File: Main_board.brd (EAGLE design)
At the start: 77.5 x 67.3 mm, 77 parts, among them IC1 4050D, U1 MCP73831, U2 TPS61200, U3 MAX1704X, U4 USD-SOCKETNEW, U5 TPS61200, X1 USB-MICROB, Y1 16MHz KX-7

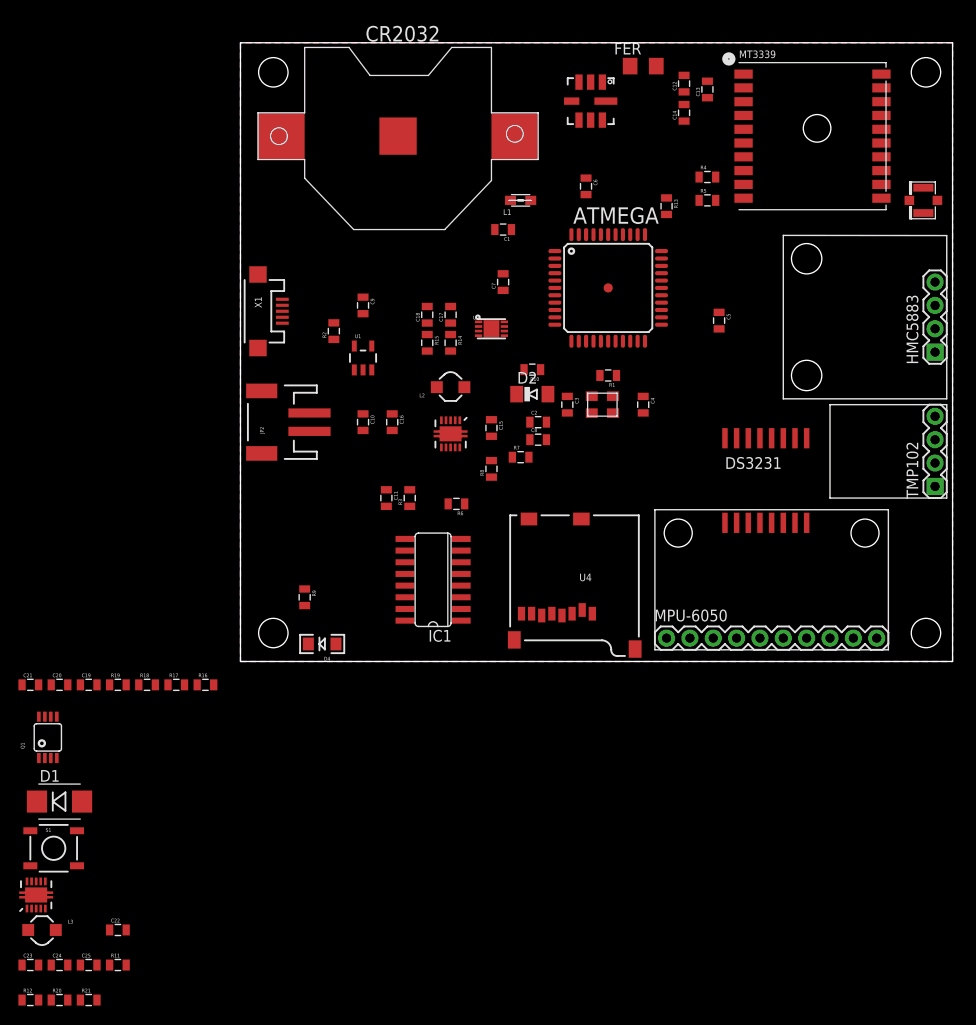
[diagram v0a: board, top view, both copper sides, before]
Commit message: Big update
Replacement of old file by only one unique file
Reorganisation of schematics
Integration of the screen footprint
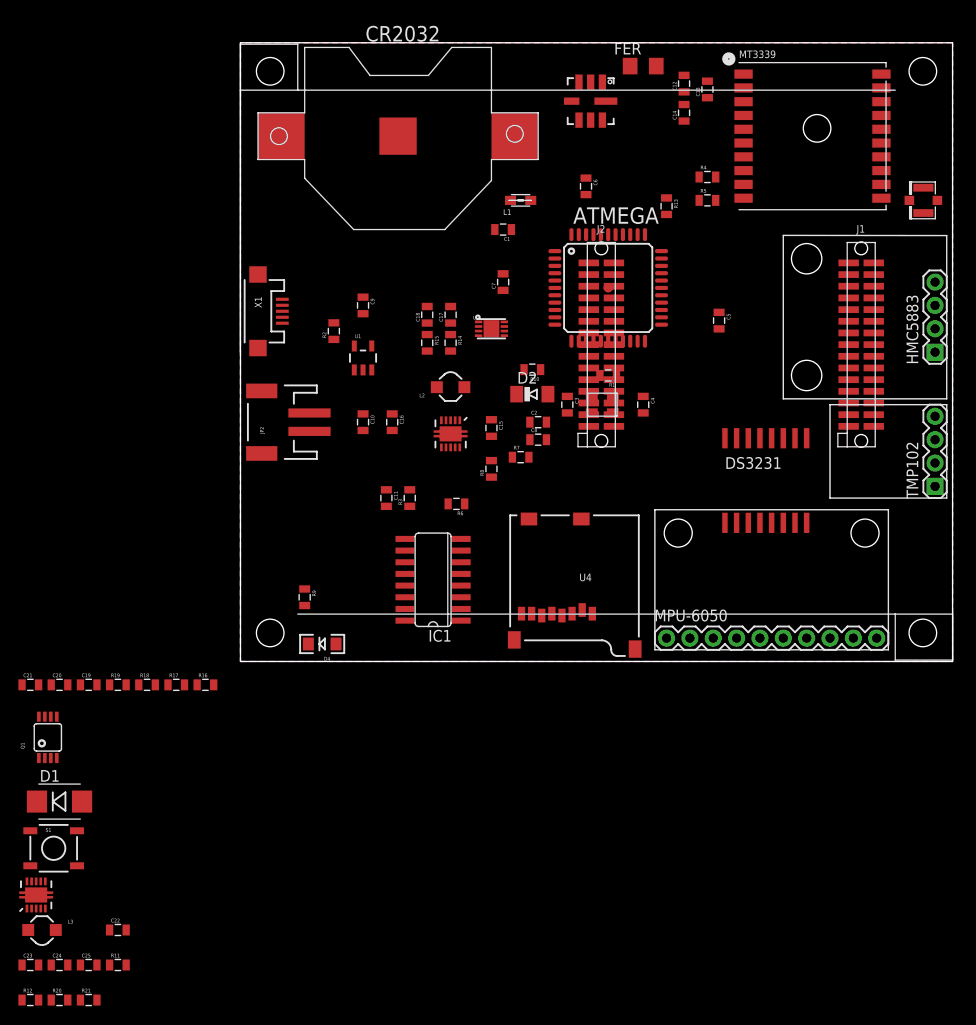
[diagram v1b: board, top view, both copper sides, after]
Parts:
- added U$2: µLCD-32PT, 4DSystems:µLCD-32PT
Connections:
- net 5V: now also U$2.J2-P6
- net GND: now also U$2.J1-P15, U$2.J2-P15, U$2.J2-P17
- net RX: now also U$2.J2-P27
- net TX: now also U$2.J2-P29
- net VCC: now also U$2.J1-P18, U$2.J2-P16, U$2.J2-P18
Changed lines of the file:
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@@
 <wire x1="64.135" y1="27.94" x2="64.135" y2="17.78" width="0.1524" layer="21"/>
 <wire x1="64.135" y1="17.78" x2="76.835" y2="17.78" width="0.1524" layer="21"/>
-<hole x="3.575" y="64.095" drill="3.2"/>
-<hole x="3.575" y="3.095" drill="3.2"/>
-<hole x="74.575" y="3.095" drill="3.2"/>
-<hole x="74.575" y="64.095" drill="3.2"/>
 </plain>
 <attributes>
@@
 <element name="C25" library="SparkFun" package="0805" value="10uF" x="-16.51" y="-33.02"/>
 <element name="L3" library="SparkFun" package="CDRH2D09" value="4.7uH, 1.2A" x="-21.59" y="-29.21"/>
+<element name="U$2" library="4DSystems" package="µLCD-32PT" value="µLCD-32PT" x="38.735" y="33.655"/>
 </elements>
 <signals>
@@
 <contactref element="U5" pad="13"/>
 <contactref element="C24" pad="2"/>
+<contactref element="U$2" pad="J2-P15"/>
+<contactref element="U$2" pad="J1-P15"/>
+<contactref element="U$2" pad="J2-P17"/>
 <wire x1="69.73" y1="51.9" x2="69.73" y2="62.4" width="0" layer="19" extent="1-1"/>
 <wire x1="74.295" y1="51.54" x2="69.73" y2="51.9" width="0" layer="19" extent="1-1"/>
@@
 <wire x1="27.675" y1="46.99" x2="28.575" y2="42.175" width="0" layer="19" extent="1-1"/>
 <wire x1="40.005" y1="40.64" x2="34.205" y2="41.44" width="0" layer="19" extent="1-1"/>
+<wire x1="40.62525" y1="35.74" x2="40.005" y2="40.64" width="0" layer="19" extent="1-1"/>
+<wire x1="40.62525" y1="34.47" x2="40.62525" y2="35.74" width="0" layer="19" extent="1-1"/>
+<wire x1="38.405" y1="34.84" x2="40.62525" y2="34.47" width="0" layer="19" extent="1-1"/>
+<wire x1="45.805" y1="36.64" x2="40.62525" y2="35.74" width="0" layer="19" extent="1-1"/>
 <wire x1="25.905" y1="36.945" x2="28.575" y2="42.175" width="0" layer="19" extent="1-1"/>
 <wire x1="25.905" y1="35.445" x2="25.905" y2="36.945" width="0" layer="19" extent="1-1"/>
@@
 <wire x1="22.86" y1="38.619" x2="25.905" y2="36.945" width="0" layer="19" extent="1-1"/>
 <wire x1="20.32" y1="38.619" x2="22.86" y2="38.619" width="0" layer="19" extent="1-1"/>
-<wire x1="38.405" y1="34.84" x2="40.005" y2="40.64" width="0" layer="19" extent="1-1"/>
 <wire x1="38.22" y1="28.865" x2="38.405" y2="34.84" width="0" layer="19" extent="1-1"/>
 <wire x1="35.56" y1="28.84" x2="38.22" y2="28.865" width="0" layer="19" extent="1-1"/>
@@
 <wire x1="7.51" y1="25.035" x2="13.335" y2="25.135" width="0" layer="19" extent="1-1"/>
 <wire x1="37.592" y1="52.589" x2="36.805" y2="46.44" width="0" layer="19" extent="1-1"/>
+<wire x1="52.07" y1="36.184" x2="45.805" y2="36.64" width="0" layer="19" extent="1-1"/>
 <wire x1="13.335" y1="31.7199" x2="13.335" y2="25.135" width="0" layer="19" extent="1-1"/>
 <wire x1="10.16" y1="36.841" x2="13.335" y2="31.7199" width="0" layer="19" extent="1-1"/>
 <wire x1="13.335" y1="37.835" x2="10.16" y2="36.841" width="0" layer="19" extent="1-1"/>
 <wire x1="4.555" y1="36.8" x2="10.16" y2="36.841" width="0" layer="19" extent="1-1"/>
-<wire x1="45.805" y1="36.64" x2="40.005" y2="40.64" width="0" layer="19" extent="1-1"/>
-<wire x1="52.07" y1="36.184" x2="45.805" y2="36.64" width="0" layer="19" extent="1-1"/>
 <wire x1="31.387" y1="15.5004" x2="33.285" y2="24.13" width="0" layer="19" extent="1-1"/>
 <wire x1="37.087" y1="15.5004" x2="31.387" y2="15.5004" width="0" layer="19" extent="1-1"/>
@@
 <wire x1="59.055" y1="15.085" x2="60.325" y2="15.085" width="0" layer="19" extent="1-1"/>
 <wire x1="57.785" y1="15.085" x2="59.055" y2="15.085" width="0" layer="19" extent="1-1"/>
+<wire x1="68.89525" y1="34.47" x2="61.595" y2="24.285" width="0" layer="19" extent="1-1"/>
+<wire x1="75.565" y1="33.655" x2="68.89525" y2="34.47" width="0" layer="19" extent="1-1"/>
+<wire x1="75.565" y1="26.67" x2="75.565" y2="33.655" width="0" layer="19" extent="1-1"/>
 <wire x1="66.675" y1="2.54" x2="61.595" y2="15.085" width="0" layer="19" extent="1-1"/>
-<wire x1="75.565" y1="26.67" x2="61.595" y2="24.285" width="0" layer="19" extent="1-1"/>
-<wire x1="75.565" y1="33.655" x2="75.565" y2="26.67" width="0" layer="19" extent="1-1"/>
 <wire x1="17.145" y1="57.15" x2="27.675" y2="46.99" width="0" layer="19" extent="1-1"/>
 <wire x1="-21.28" y1="-6.005" x2="17.8816" y2="6.985" width="0" layer="19" extent="1-1"/>
@@
 <contactref element="R10" pad="2"/>
 <contactref element="U$1" pad="3"/>
+<contactref element="U$2" pad="J2-P16"/>
+<contactref element="U$2" pad="J1-P18"/>
+<contactref element="U$2" pad="J2-P18"/>
+<wire x1="66.16475" y1="35.74" x2="75.565" y2="36.195" width="0" layer="19" extent="1-1"/>
 <wire x1="75.565" y1="19.05" x2="75.565" y2="36.195" width="0" layer="19" extent="1-1"/>
 <wire x1="69.215" y1="2.54" x2="75.565" y2="19.05" width="0" layer="19" extent="1-1"/>
@@
 <wire x1="23.36" y1="26.24" x2="30.05" y2="29.083" width="0" layer="19" extent="1-1"/>
 <wire x1="37.605" y1="34.84" x2="30.85" y2="31.75" width="0" layer="19" extent="1-1"/>
-<wire x1="34.205" y1="43.84" x2="37.605" y2="34.84" width="0" layer="19" extent="1-1"/>
+<wire x1="37.89475" y1="34.47" x2="37.605" y2="34.84" width="0" layer="19" extent="1-1"/>
+<wire x1="37.89475" y1="35.74" x2="37.605" y2="34.84" width="0" layer="19" extent="1-1"/>
+<wire x1="34.205" y1="43.84" x2="37.89475" y2="35.74" width="0" layer="19" extent="1-1"/>
 <wire x1="29.475" y1="46.99" x2="34.205" y2="43.84" width="0" layer="19" extent="1-1"/>
 <wire x1="29.38" y1="50.165" x2="29.475" y2="46.99" width="0" layer="19" extent="1-1"/>
@@
 <contactref element="R4" pad="1"/>
 <contactref element="ATMEGA" pad="21"/>
-<wire x1="43.205" y1="34.84" x2="49.9" y2="52.705" width="0" layer="19" extent="1-1"/>
+<contactref element="U$2" pad="J2-P29"/>
+<wire x1="40.62525" y1="43.36" x2="49.9" y2="52.705" width="0" layer="19" extent="1-1"/>
+<wire x1="43.205" y1="34.84" x2="40.62525" y2="43.36" width="0" layer="19" extent="1-1"/>
 </signal>
 <signal name="RX">
 <contactref element="R5" pad="1"/>
 <contactref element="ATMEGA" pad="20"/>
-<wire x1="42.405" y1="34.84" x2="49.9" y2="50.165" width="0" layer="19" extent="1-1"/>
+<contactref element="U$2" pad="J2-P27"/>
+<wire x1="40.62525" y1="42.09" x2="49.9" y2="50.165" width="0" layer="19" extent="1-1"/>
+<wire x1="42.405" y1="34.84" x2="40.62525" y2="42.09" width="0" layer="19" extent="1-1"/>
 </signal>
 <signal name="VEE">
@@
 <contactref element="C22" pad="1"/>
 <contactref element="R20" pad="2"/>
-<wire x1="-14.235" y1="-29.21" x2="-18.785" y2="-36.83" width="0" layer="19" extent="1-1"/>
+<contactref element="U$2" pad="J2-P6"/>
+<wire x1="-14.235" y1="-29.21" x2="37.89475" y2="28.12" width="0" layer="19" extent="1-1"/>
 <wire x1="-22.725" y1="-26.875" x2="-14.235" y2="-29.21" width="0" layer="19" extent="1-1"/>
+<wire x1="-18.785" y1="-36.83" x2="-14.235" y2="-29.21" width="0" layer="19" extent="1-1"/>
 </signal>
 <signal name="EN5V">
@@
 </board>
 </drawing>
+<compatibility>
+<note version="6.3" minversion="6.2.2" severity="warning">
+Since Version 6.2.2 text objects can contain more than one line,
+which will not be processed correctly with this version.
+</note>
+</compatibility>
 </eagle>

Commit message: Final design
Board routed and schematics finalised and cleaned
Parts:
- removed C23: 0.1uF, SparkFun:0805
- removed C25: 10uF, SparkFun:0805
- removed HMC5883, TMP102: (no value), SparkFun:1X04
- removed JP1, JP5: STAND-OFF, SparkFun:STAND-OFF
- removed JP7, JP8: STAND-OFFTIGHT, SparkFun:STAND-OFF-TIGHT
- removed MPU-6050: M10", SparkFun:1X10
- removed R11: 2M, SparkFun:0805
- removed R12: 220k, SparkFun:0805
- added U$6: HMC5883, SparkFun-Breakouts:HMC5883
- added U$7: MPU-6050, SparkFun-Breakouts:MPU-6050
- added U$8: TMP102, SparkFun-Breakouts:TMP102
- D1: device SparkFun-DiscreteSemi:DIODE-HV -> SparkFun-DiscreteSemi:SMA-DIODE_ALT
- S1: value SWITCH-MOMENTARY-2SMD -> (none)
- moved S1 81.6 mm to (3.17, 57.8), flipped to the bottom, turned to 90 degrees
- moved R21 77.3 mm to (16.5, 33.0), flipped to the bottom
- moved R20 75.1 mm to (9.53, 32.4), flipped to the bottom, turned to 90 degrees
- moved L3 74.1 mm to (10.8, 37.5), flipped to the bottom, turned to 90 degrees
- moved C24 73.3 mm to (13.3, 32.4), flipped to the bottom, turned to 270 degrees
- moved U5 71.8 mm to (14.6, 36.2), flipped to the bottom, turned to 90 degrees
- moved D1 71.3 mm to (3.81, 52.1), flipped to the bottom
- moved C22 66.4 mm to (11.4, 32.4), flipped to the bottom, turned to 270 degrees
- moved D4 64.9 mm to (19.1, 66.0)
- moved Q1 54.5 mm to (4.45, 40.0), flipped to the bottom
- moved C19 54.4 mm to (1.27, 48.9), flipped to the bottom, turned to 270 degrees
- moved R9 52.9 mm to (21.6, 57.8), flipped to the bottom, turned to 90 degrees
- moved R16 52.0 mm to (3.81, 48.9), flipped to the bottom, turned to 270 degrees
- moved C20 52.0 mm to (2.54, 44.5), flipped to the bottom, turned to 180 degrees
- moved R17 49.8 mm to (2.54, 46.4), flipped to the bottom, turned to 180 degrees
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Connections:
- removed net +3V3: IC1.1, U4.4
- removed net EN5V: U5.6
- removed net IOPIN: D1.A, R18.1, R19.1
- removed net UVLO1: C23.2, R11.1, R12.2, U5.7
- net A5: now also U5.6
- net AUX_SCL: now also U$6.SCL, U$7.AUX_SCL; no longer HMC5883.4, MPU-6050.2
- net AUX_SDA: now also U$6.SDA, U$7.AUX_SDA; no longer HMC5883.3, MPU-6050.1
- net CLKIN: now also U$7.CLK; no longer MPU-6050.3
- net D7: now also D1.A, R18.1, R19.1
- net FSYNC: now also U$7.FSYNC; no longer MPU-6050.7
- net GND: now also S1.2, U$6.GND, U$7.GND, U$8.ADD0, U$8.GND; no longer C25.2, HMC5883.1, MPU-6050.9, TMP102.4
- net GND1: no longer R12.1
- net INT: now also U$7.INT; no longer MPU-6050.8
- net IO10*: now also IC1.3; no longer IC1.7
- net IO13*: now also IC1.7; no longer IC1.3
- net N$12: now also IC1.6; no longer IC1.2
- net N$13: now also IC1.2; no longer IC1.6
- net N$18: now also S1.4
- net SCL: now also U$7.SCL, U$8.SCL; no longer MPU-6050.6, TMP102.3
- net SDA: now also U$7.SDA, U$8.SDA; no longer MPU-6050.5, TMP102.2
- net VCC: now also IC1.1, U$6.VCC, U$7.VDD, U$8.V+, U4.4; no longer HMC5883.2, MPU-6050.10, TMP102.1
- net VIN: now also U5.7; no longer C23.1, C25.1, R11.2
- net VIO: now also U$7.VIO; no longer MPU-6050.4
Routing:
- net VCC: track 0.00 -> 254.0 mm, vias 0 -> 9
- net SDA: track 0.00 -> 141.7 mm, vias 0 -> 5
- net SCL: track 0.00 -> 140.9 mm, vias 0 -> 7
- net VEE: track 0.00 -> 84.7 mm, vias 0 -> 1
- net VUSB: track 0.00 -> 73.4 mm, vias 0 -> 3
- net VIN: track 0.00 -> 60.1 mm, vias 0 -> 2
- net TX: track 0.00 -> 54.8 mm, vias 0 -> 4
- net AUX_SDA: track 0.00 -> 53.6 mm
- net RX: track 0.00 -> 51.8 mm, vias 0 -> 2
- net AUX_SCL: track 0.00 -> 49.2 mm
- net FB: track 0.00 -> 45.6 mm, vias 0 -> 2
- net RD+: track 0.00 -> 41.5 mm, vias 0 -> 2
- net IO12: track 0.00 -> 39.5 mm, vias 0 -> 3
- net D7: track 0.00 -> 38.8 mm, vias 0 -> 2
- net RD-: track 0.00 -> 38.3 mm, vias 0 -> 2
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
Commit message: Board clean up
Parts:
- renumbered IC1 to 4050D, U1 to MCP73831

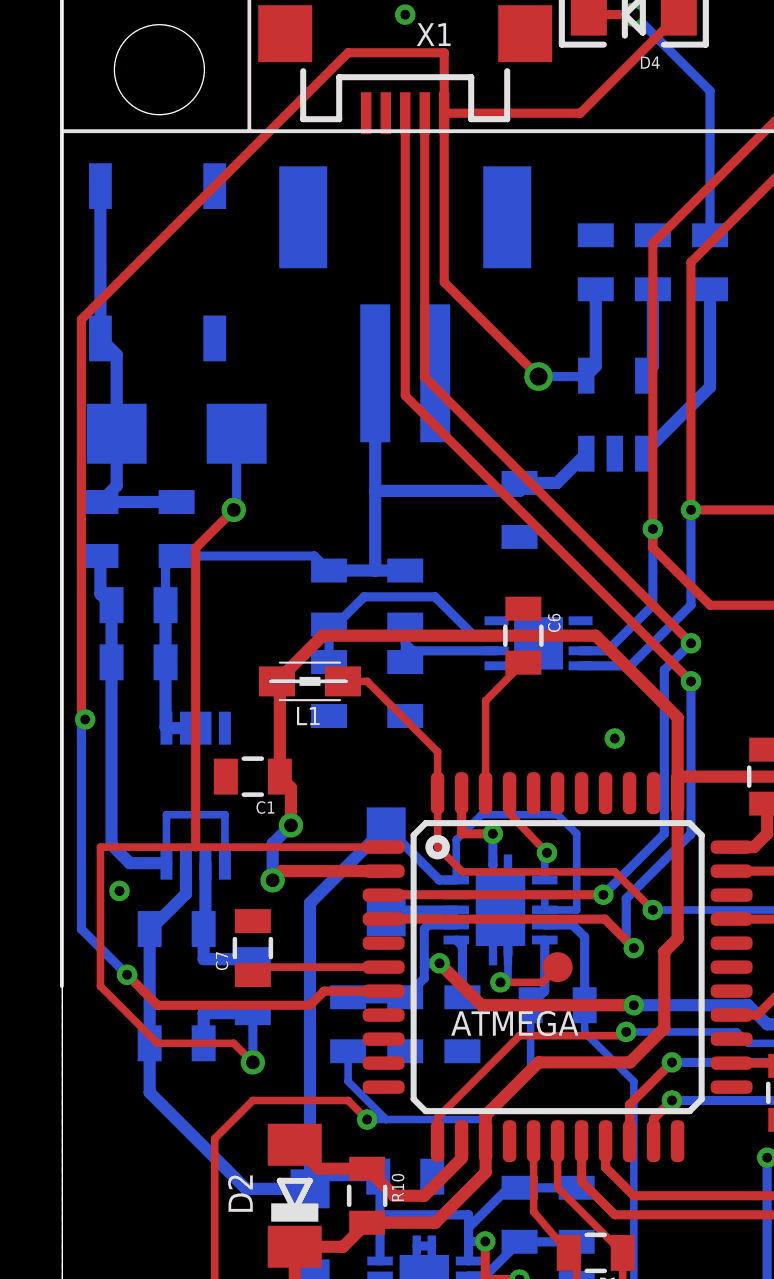
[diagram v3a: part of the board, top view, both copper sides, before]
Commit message: Maxim library update + ON/OFF switch mod
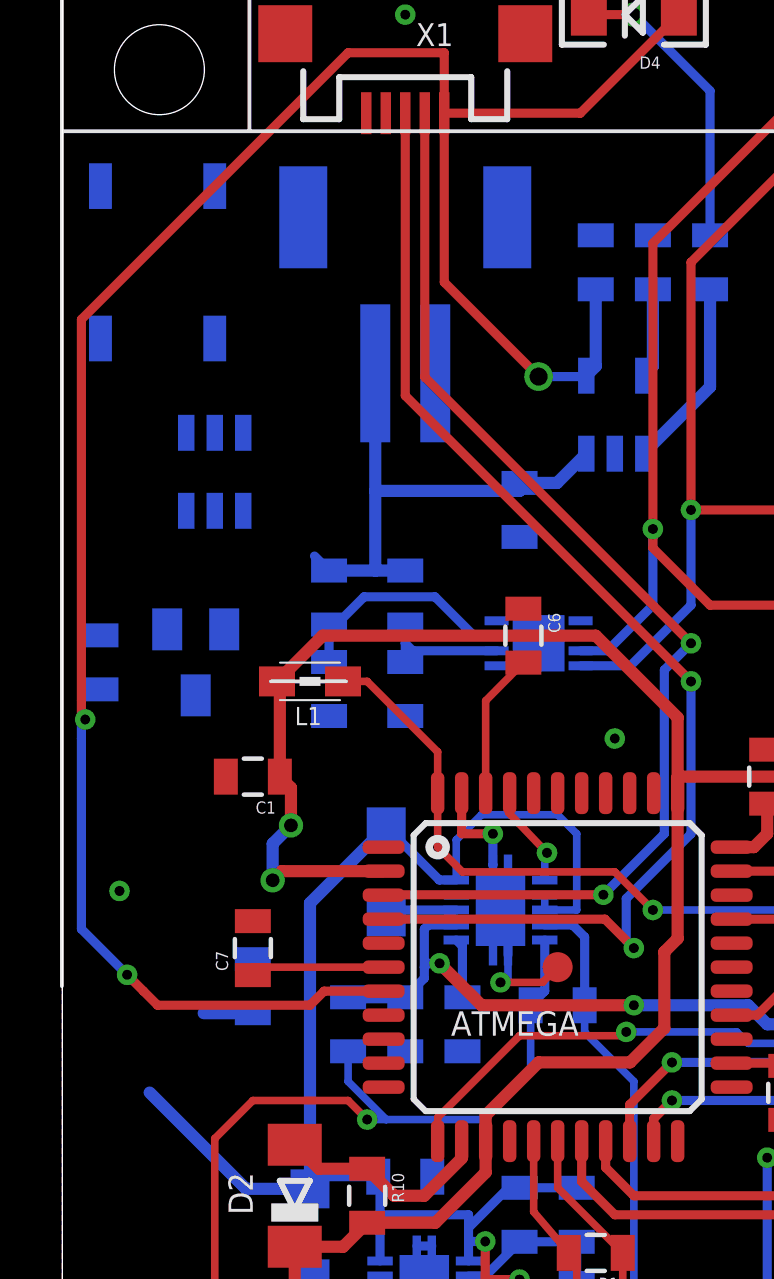
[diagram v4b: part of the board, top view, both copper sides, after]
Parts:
- removed C19: 1µ, SparkFun-Passives:0805
- removed C20: 0.1µ, SparkFun-Passives:0805
- removed C21: 10µ, SparkFun-Passives:0805
- removed D1: (no value), SparkFun-DiscreteSemi:SMA-DIODE_ALT
- removed Q1: (no value), SparkFun-DiscreteSemi:MSOP8
- removed R16: 10k, SparkFun-Passives:0805
- removed R17, R19: 100k, SparkFun-Passives:0805
- added Q2: (no value), dp_devices:SOT-23
- added R11: 300k, SparkFun-Passives:0805
- added U$9: MAX16054, maxim:SOT23-6L
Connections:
- removed net N$18: C19.1, D1.C, R16.1, S1.3, S1.4
- removed net N$20: C19.2, C20.1, Q1.1, Q1.4, R17.1
- new net N$19: Q2.1, R11.2, U$9.4
- net D7: now also U$9.3; no longer D1.A, R19.1
- net GND: now also R18.2, S1.3, S1.4, U$9.2; no longer Q1.7, Q1.8, S1.1, S1.2
- net N$15: now also S1.1, S1.2, U$9.1; no longer C21.1, Q1.2, R18.2
- net VCC: now also U$9.6
- net VIN: now also Q2.2; no longer C21.2, Q1.3, R19.2
- net V_BATT: now also Q2.3, R11.1; no longer C20.2, Q1.5, Q1.6, R16.2, R17.2
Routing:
- net D7: track 38.8 -> 1.64 mm, vias 2 -> 0
- net N$20: track 17.0 -> 0.00 mm
- net N$18: track 13.5 -> 0.00 mm
- net V_BATT: track 28.7 -> 17.5 mm
- net VIN: track 60.1 -> 51.9 mm
- net N$15: track 4.90 -> 0.00 mm
